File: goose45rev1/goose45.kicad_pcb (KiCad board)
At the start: 2 copper layers, 247 x 74.8 mm, 141 parts, among them J1 USB_C_Receptacle_USB2.0, J2 SPI, J3 Debugger, J4 USB connector, J5 USART, SW1 Conn_01x02_Female, SW10 SW_Push, SW11 SW_Push, SW12 SW_Push, SW13 SW_Push, SW14 SW_Push, SW15 SW_Push, SW16 SW_Push, SW17 SW_Push, SW18 SW_Push, SW19 SW_Push, SW2 SW_Push, SW20 SW_Push, SW21 SW_Push, SW22 SW_Push, SW23 SW_Push, SW24 SW_Push, SW25 SW_Push, SW26 SW_Push, SW27 SW_Push, SW28 SW_Push, SW29 SW_Push, SW3 SW_Push, SW30 SW_Push, SW31 SW_Push, SW32 SW_Push, SW33 SW_Push, SW34 SW_Push, SW35 SW_Push, SW36 SW_Push, SW37 SW_Push, SW38 SW_Push, SW39 SW_Push, SW4 SW_Push, SW40 SW_Push, SW41 SW_Push, SW42 SW_Push, SW43 SW_Push, SW44 SW_Push, SW45 SW_Push, SW46 SW_Push, SW48 SW_Push, SW5 SW_Push, SW6 SW_Push, SW7 SW_Push, SW8 SW_Push, SW9 SW_Push, U1 STM32F103CBTx, U2 USBLC6-2SC6, U3 TLV75533PDBV, X1 Crystal_GND24

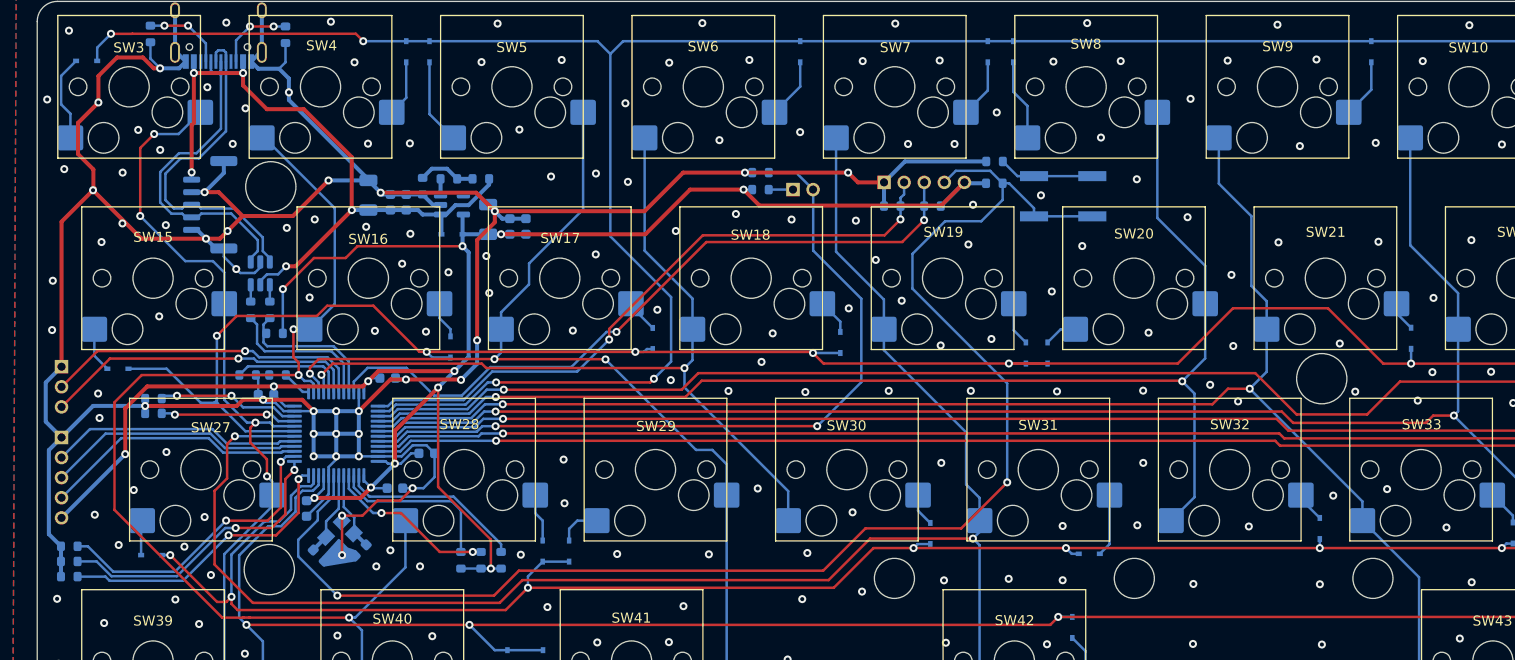
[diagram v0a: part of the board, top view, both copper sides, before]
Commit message: update goose45 pcb usb pad and crystal
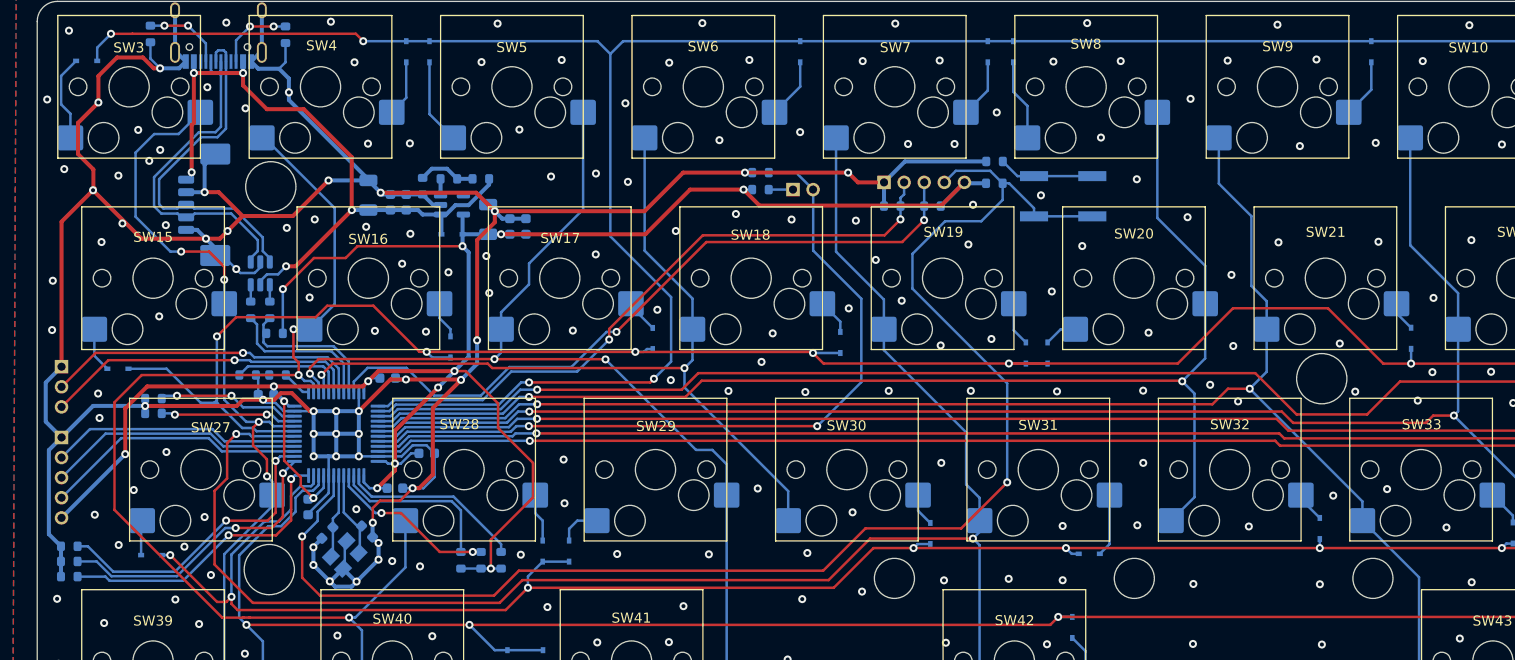
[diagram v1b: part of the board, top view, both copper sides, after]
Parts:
- J4: footprint Connector_Molex:Molex_CLIK-Mate_502386-0570_1x05-1MP_P1.25mm_Horizontal -> Connector_Molex:Molex_PicoBlade_53261-0571_1x05-1MP_P1.25mm_Horizontal
- moved C7 2.42 mm to (55.1, 111.4), turned to -135 degrees
- moved X1 2.02 mm to (56.8, 113.6)
- moved C6 1.98 mm to (59.1, 111.2), turned to -45 degrees
- moved C2 0.21 mm to (53.2, 108.8)
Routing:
- net GND: track 367.5 -> 392.4 mm, vias 310 -> 315
- net +3.3V: track 213.0 -> 222.5 mm, vias 13 -> 14
- net /Interface/USBD+: track 34.6 -> 35.6 mm
- net /Interface/USBD-: track 34.9 -> 35.9 mm
- net col1: track 75.0 -> 76.0 mm
- net XTAL1: track 7.91 -> 8.83 mm
- net RESET: track 143.4 -> 144.1 mm

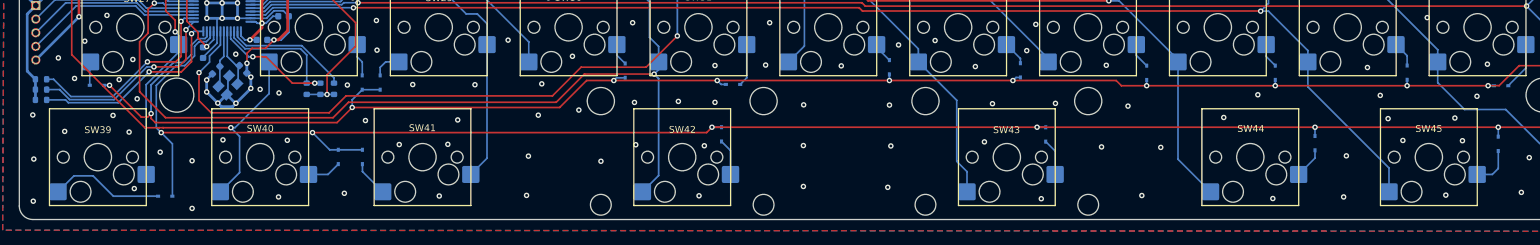
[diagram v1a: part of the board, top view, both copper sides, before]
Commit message: Change goose45 mod key size
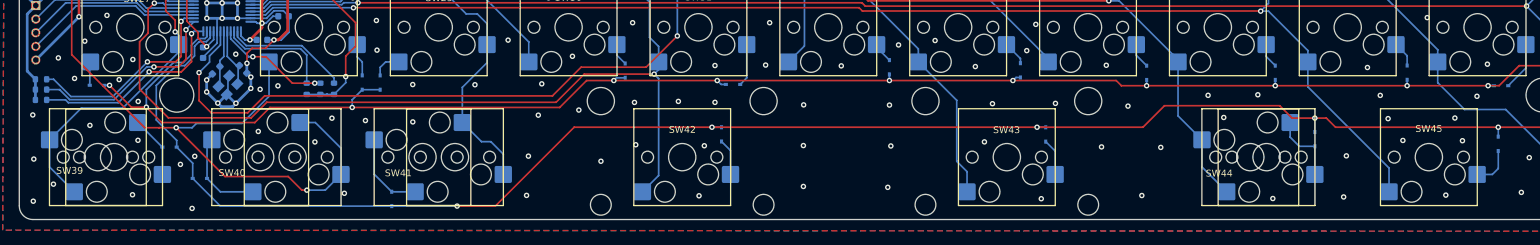
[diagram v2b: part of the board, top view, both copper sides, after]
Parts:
- added SW39_1: SW_Push, Switch_Keyboard_Hotswap_Kailh.pretty:SW_Hotswap_Kailh_MX, F.Cu at (40.1, 124.1)
- added SW40_1: SW_Push, Switch_Keyboard_Hotswap_Kailh.pretty:SW_Hotswap_Kailh_MX, F.Cu at (66.3, 124.1)
- added SW41_1: SW_Push, Switch_Keyboard_Hotswap_Kailh.pretty:SW_Hotswap_Kailh_MX, F.Cu at (90.1, 124.1)
- added SW44_1: SW_Push, Switch_Keyboard_Hotswap_Kailh.pretty:SW_Hotswap_Kailh_MX, F.Cu at (209.2, 124.1)
- moved D40 20.6 mm to (52.7, 127.3), turned to 0 degrees
- moved D41 7.51 mm to (80.9, 130.3), turned to 90 degrees
- moved D39 7.23 mm to (48.3, 122.7)
- moved D44 0.58 mm to (216.3, 121.5)
- turned SW39 to 0 degrees
- turned SW40 to 0 degrees
- turned SW41 to 0 degrees
- turned SW44 to 0 degrees
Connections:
- D44 pad 2: Net-(D44-Pad2) -> Net-(SW44_1-Pad1)
- SW41 pad 1: col3 -> Net-(D41-Pad2)
- SW41 pad 2: Net-(D41-Pad2) -> col3
- SW44 pad 1: Net-(D44-Pad2) -> col9
- SW44 pad 2: col9 -> Net-(SW44_1-Pad1)
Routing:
- net col2: track 113.7 -> 143.1 mm, vias 3 -> 4
- net col1: track 76.0 -> 89.5 mm
- net Net-(SW44_1-Pad1): track 0.00 -> 10.5 mm
- net Net-(D40-Pad2): track 5.00 -> 13.5 mm
- net Net-(D39-Pad2): track 16.9 -> 9.13 mm
- net Net-(D41-Pad2): track 5.29 -> 12.1 mm
- net row4: track 305.8 -> 301.0 mm, vias 7 -> 6
- net Net-(D44-Pad2): track 4.54 -> 0.00 mm
- net col3: track 100.3 -> 104.1 mm
- net row3: track 264.6 -> 263.1 mm
- net col9: track 193.6 -> 194.6 mm
- net GND: vias 315 -> 312

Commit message: update pcb
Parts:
- moved D48 3.03 mm to (268.3, 79.6)
- moved R12 2.00 mm to (31.4, 114.2)
- moved R5 2.00 mm to (31.4, 112.7)
- moved R6 2.00 mm to (31.4, 115.7)
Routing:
- net Net-(D48-Pad2): track 7.35 -> 10.2 mm
- net PA4: track 30.4 -> 28.4 mm
- net PA2: track 29.9 -> 27.9 mm
- net PA3: track 29.5 -> 27.5 mm
- net GND: track 392.4 -> 393.9 mm, vias 312 -> 313
- net row4: track 301.0 -> 300.1 mm
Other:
- outline, holes or cut-outs redrawn
